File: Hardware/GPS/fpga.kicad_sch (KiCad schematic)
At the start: 1 part, among them U2 TI60F100S3F2I3

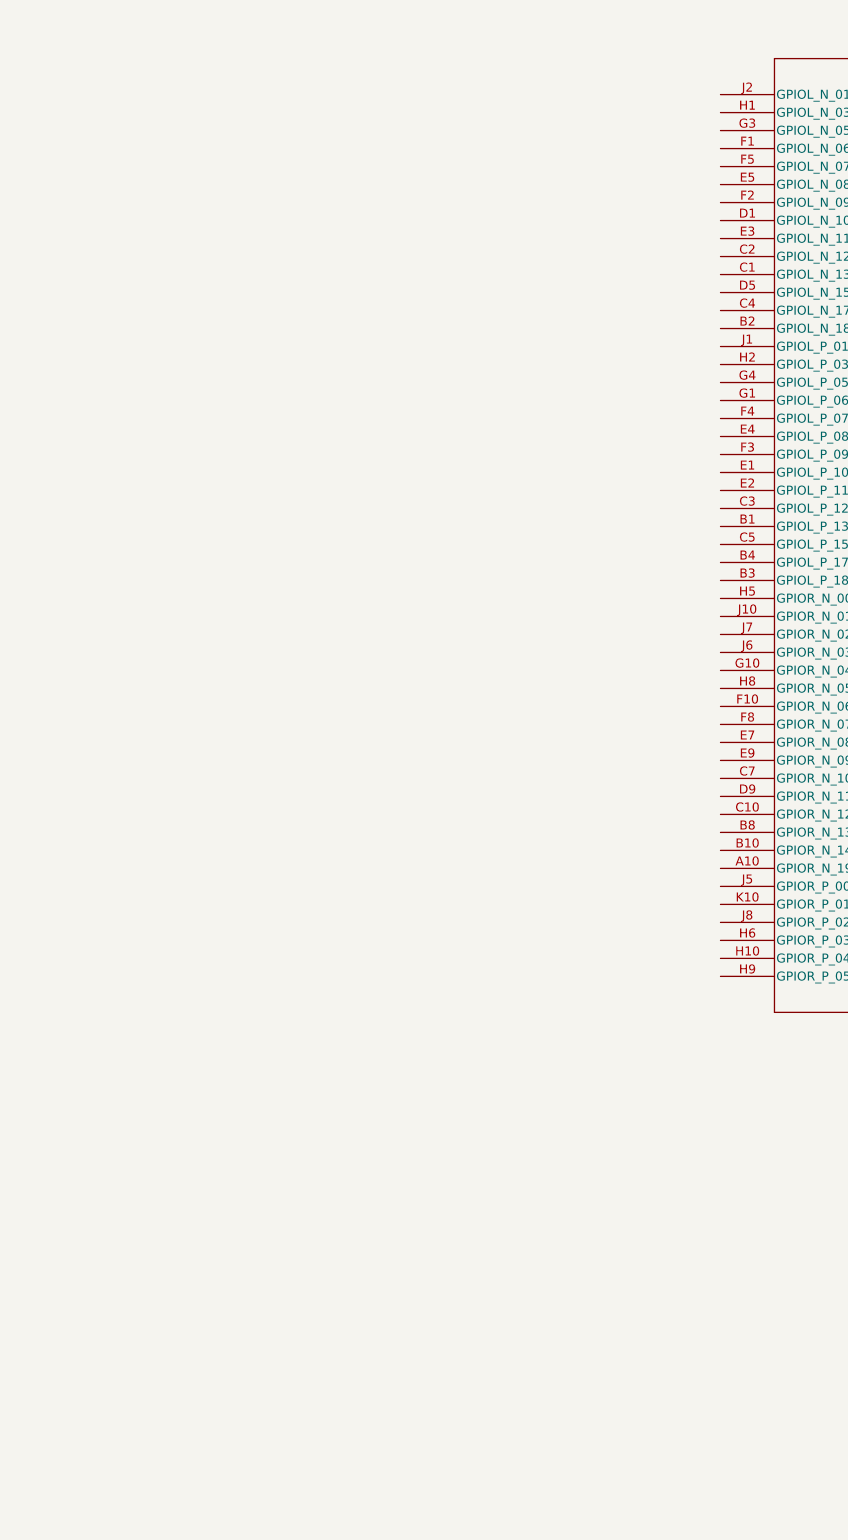
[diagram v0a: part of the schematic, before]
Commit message: Add cfg flash to schematic
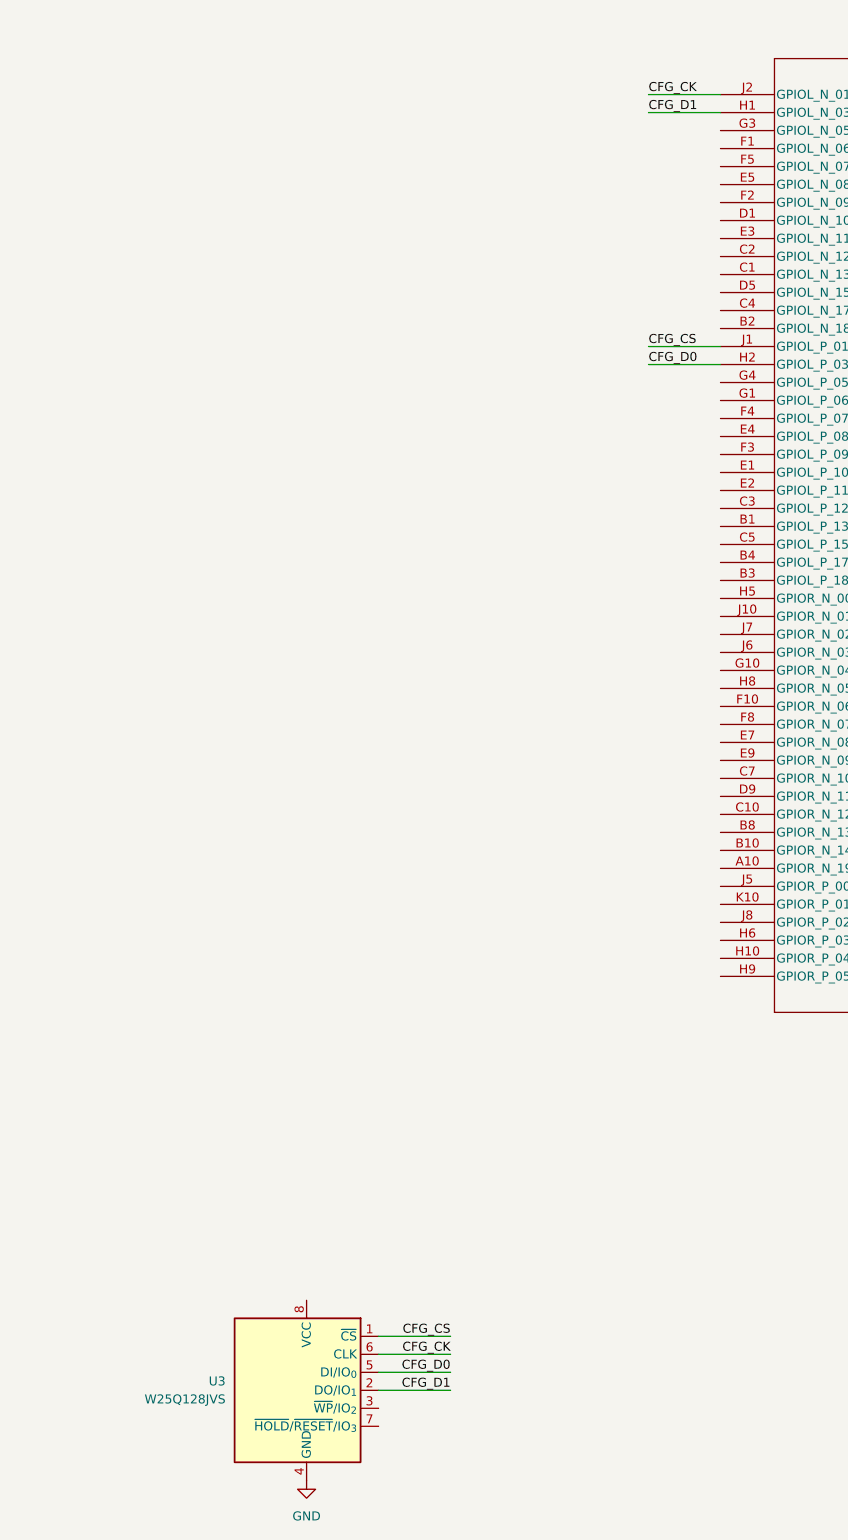
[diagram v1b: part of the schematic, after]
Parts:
- added U3: W25Q128JVS, Package_SO:SOIC-8_5.3x5.3mm_P1.27mm, symbol Memory_Flash:W25Q128JVS
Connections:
- net GND: now also U3.4 (GND)
- net CFG_D1: now reaches U2.H1 (GPIOL_N_03_CDI1)
- net CFG_D1: now also U3.2 (DO/IO_{1})
- net CFG_D0: now reaches U2.H2 (GPIOL_P_03_CDI0)
- net CFG_D0: now also U3.5 (DI/IO_{0})
- net CFG_CS: now reaches U2.J1 (GPIOL_P_01_SSL_N)
- net CFG_CS: now also U3.1 (~{CS})
- net CFG_CK: now reaches U2.J2 (GPIOL_N_01_CCK)
- net CFG_CK: now also U3.6 (CLK)

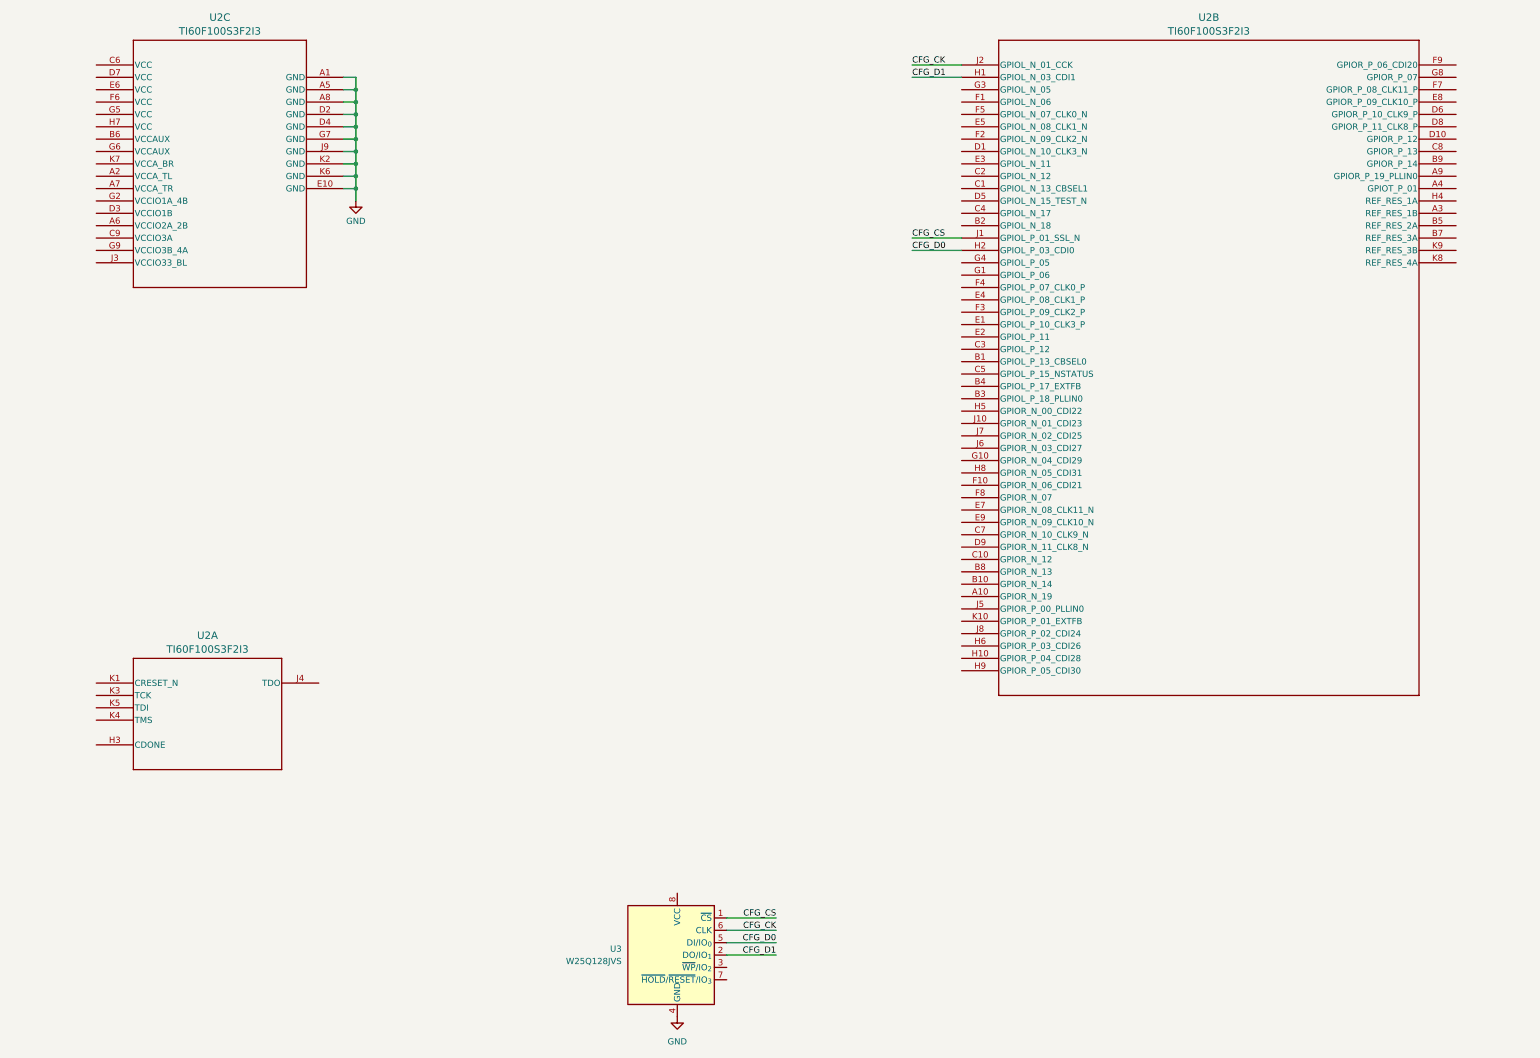
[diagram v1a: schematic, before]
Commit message: Major updates to Simulator and hardware
- Simulator has functional acquisition for L1CA, E1C, B1C, L1C.
- Simulator can track, decode, and solve for position on L1CA and E1C.
- Development on custom hardware
- Created Pi Pico 2 development environment for prototyping.
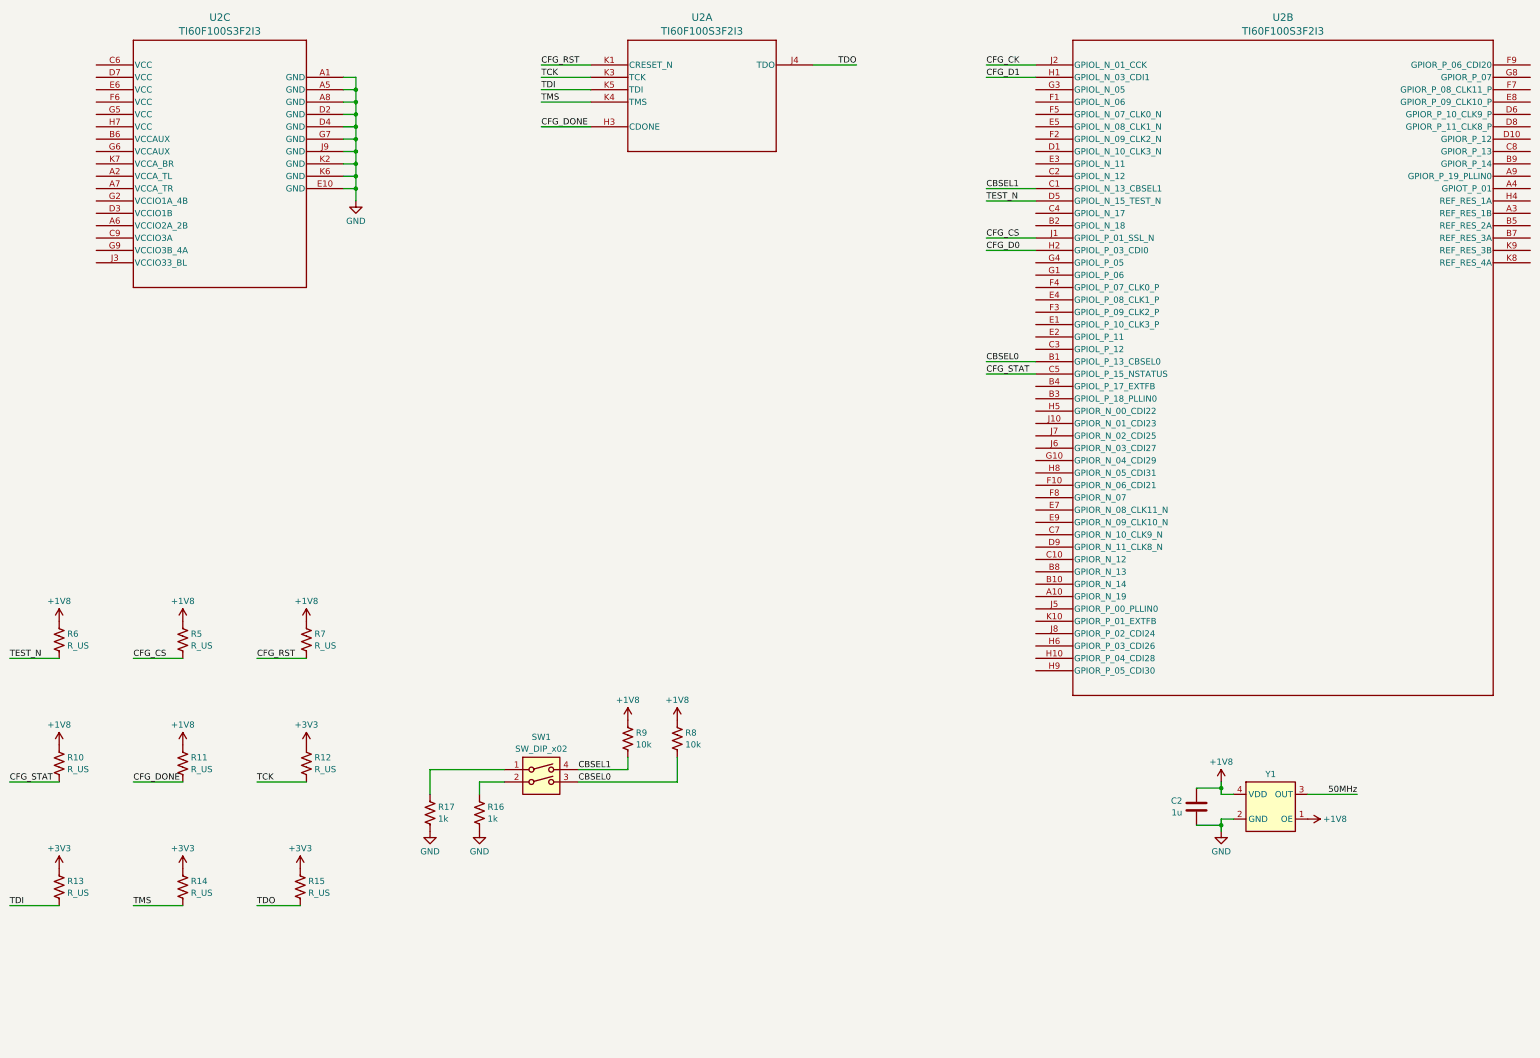
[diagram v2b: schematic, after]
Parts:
- removed U3: W25Q128JVS, Package_SO:SOIC-8_5.3x5.3mm_P1.27mm, symbol Memory_Flash:W25Q128JVS
- added C2: 1u, symbol Device:C
- added R10, R11, R12, R13, R14, R15, R5, R6, R7: R_US, symbol Device:R_US
- added R16, R17: 1k, symbol Device:R_US
- added R8, R9: 10k, symbol Device:R_US
- added SW1: SW_DIP_x02, symbol Switch:SW_DIP_x02
- added Y1: (no value), CustomFootprints:VSON_DLF-4, symbol CustomSymbols:LMK6CE050000DDLFR
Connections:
- net CFG_CS: now also R5.2
- net GND: now also C2.2, R16.2, R17.2, Y1.2 (GND)
- net CBSEL0: now reaches U2.B1 (GPIOL_P_13_CBSEL0)
- net CBSEL0: now also R8.2, SW1.3
- net CBSEL1: now reaches U2.C1 (GPIOL_N_13_CBSEL1)
- net CBSEL1: now also R9.2, SW1.4
- net CFG_STAT: now reaches U2.C5 (GPIOL_P_15_NSTATUS)
- net CFG_STAT: now also R10.2
- net TEST_N: now reaches U2.D5 (GPIOL_N_15_TEST_N)
- net TEST_N: now also R6.2
- net CFG_DONE: now reaches U2.H3 (CDONE)
- net CFG_DONE: now also R11.2
- net TDO: now reaches U2.J4 (TDO)
- net TDO: now also R15.2
- net CFG_RST: now reaches U2.K1 (CRESET_N)
- net CFG_RST: now also R7.2
- net TCK: now reaches U2.K3 (TCK)
- net TCK: now also R12.2
- net TMS: now reaches U2.K4 (TMS)
- net TMS: now also R14.2
- net TDI: now reaches U2.K5 (TDI)
- net TDI: now also R13.2
- new net: R16.1, SW1.2
- new net: R17.1, SW1.1
- new net +1V8: C2.1, R10.1, R11.1, R5.1, R6.1, R7.1, R8.1, R9.1, Y1.1 (OE), Y1.4 (VDD)
- new net +3V3: R12.1, R13.1, R14.1, R15.1
- new net 50MHz: Y1.3 (OUT)
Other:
- moved on the sheet: U2A, U2B
